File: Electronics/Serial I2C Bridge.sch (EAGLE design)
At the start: 22 parts, among them IC1 ATmega328P, Q1 16MHz

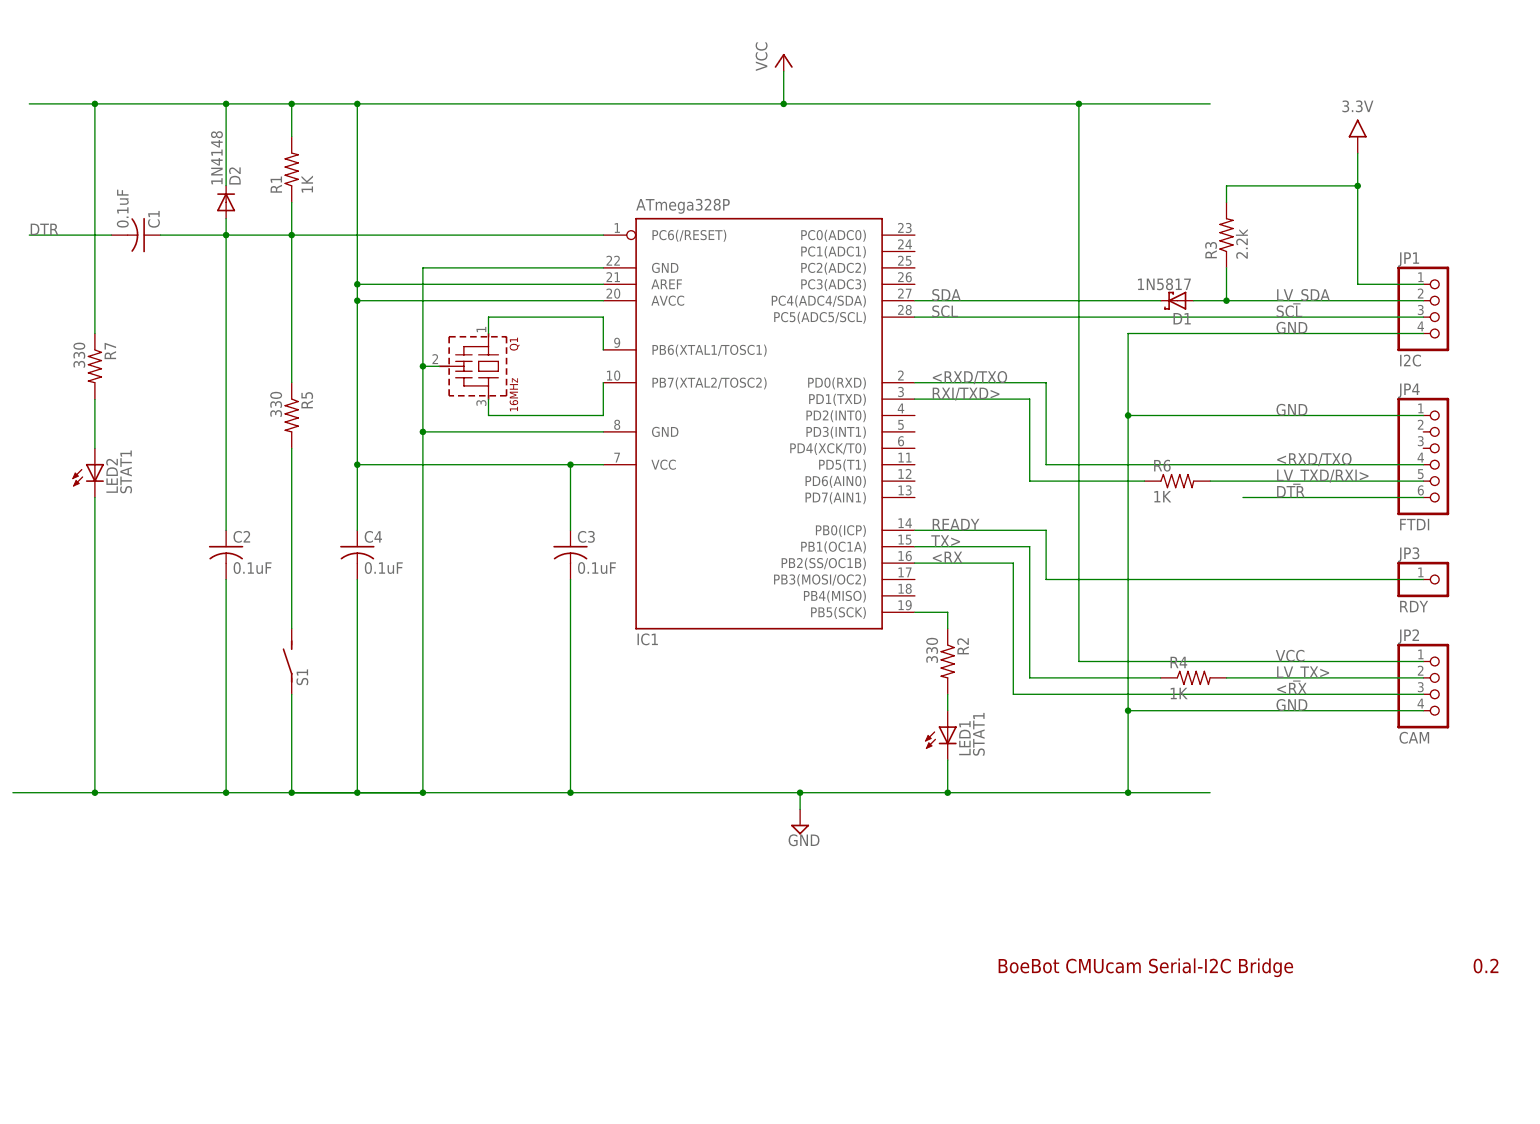
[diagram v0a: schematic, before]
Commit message: Revised level shift circuit
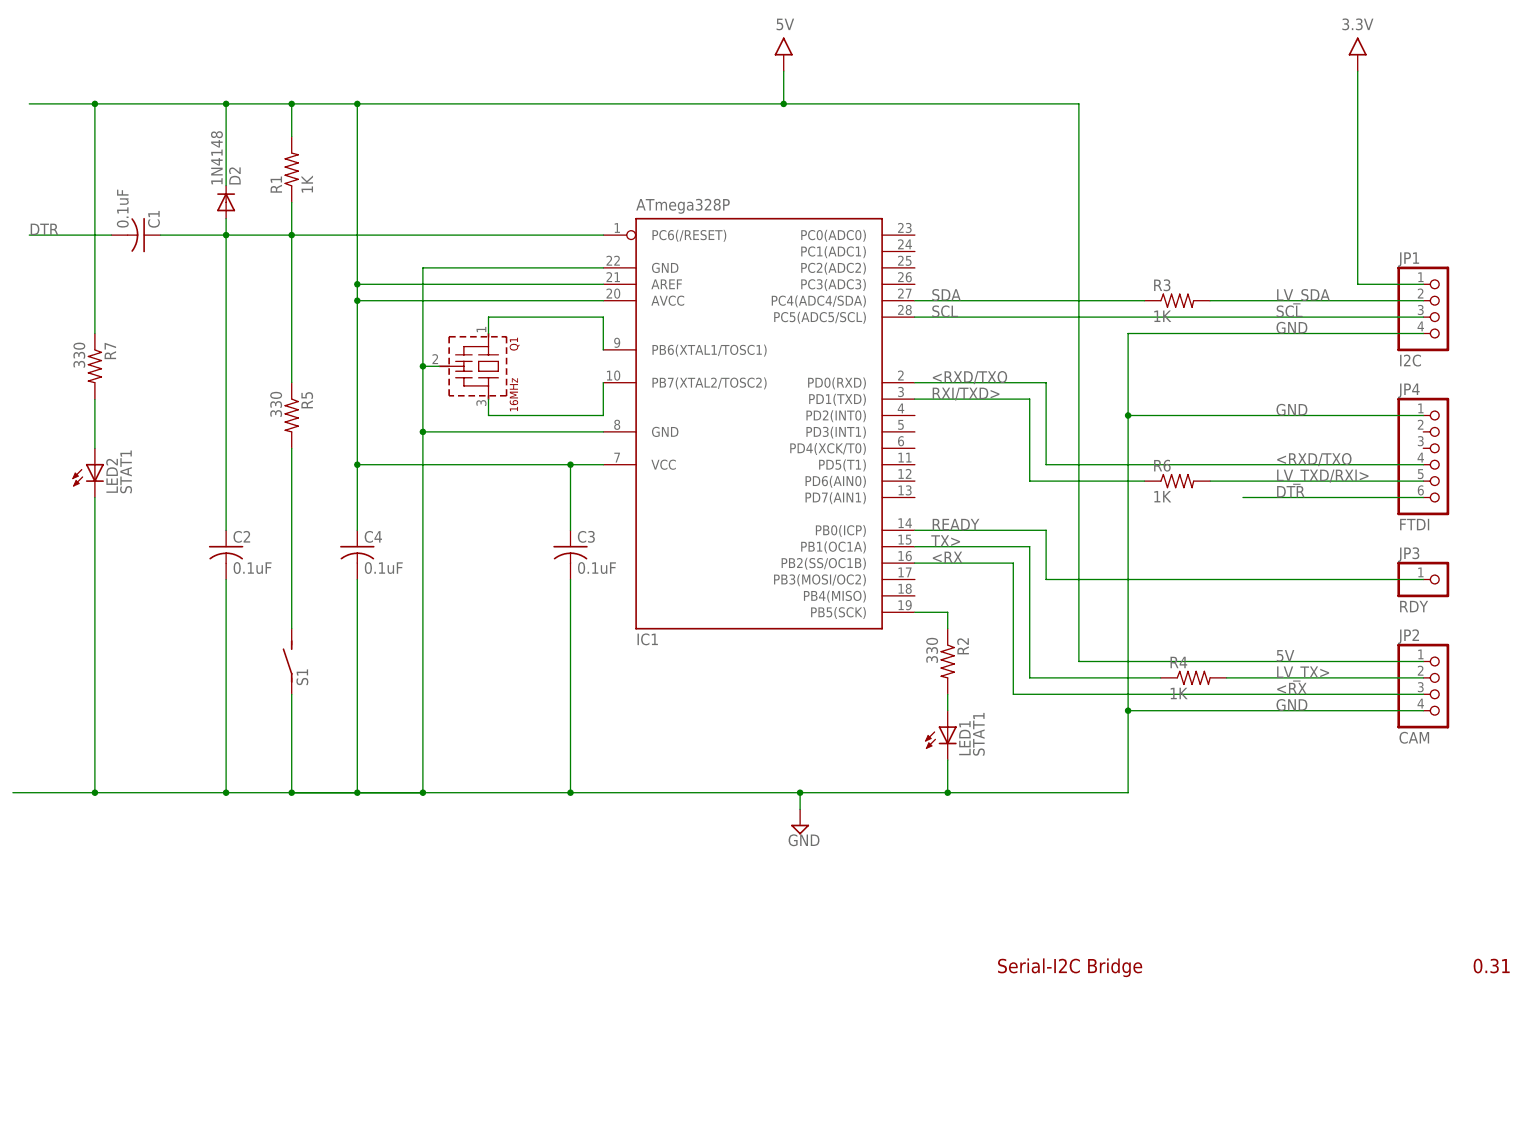
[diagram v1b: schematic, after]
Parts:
- removed D1: 1N5817, diode:1N5817-B
- R3: value 2.2k -> 1K
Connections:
- net VCC renamed 5V
- net 3.3V: no longer R3.2
- net LV_SDA: now also R3.2; no longer D1.A, R3.1
- net SDA: now also R3.1; no longer D1.C
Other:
- note added: "0.31"
- note added: "Serial-I2C Bridge"
- note removed: "0.2"
- note removed: "BoeBot CMUcam Serial-I2C Bridge"
- moved on the sheet: R3

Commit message: Moved RC Mux to subdirectory. Minor changes to various other boards.
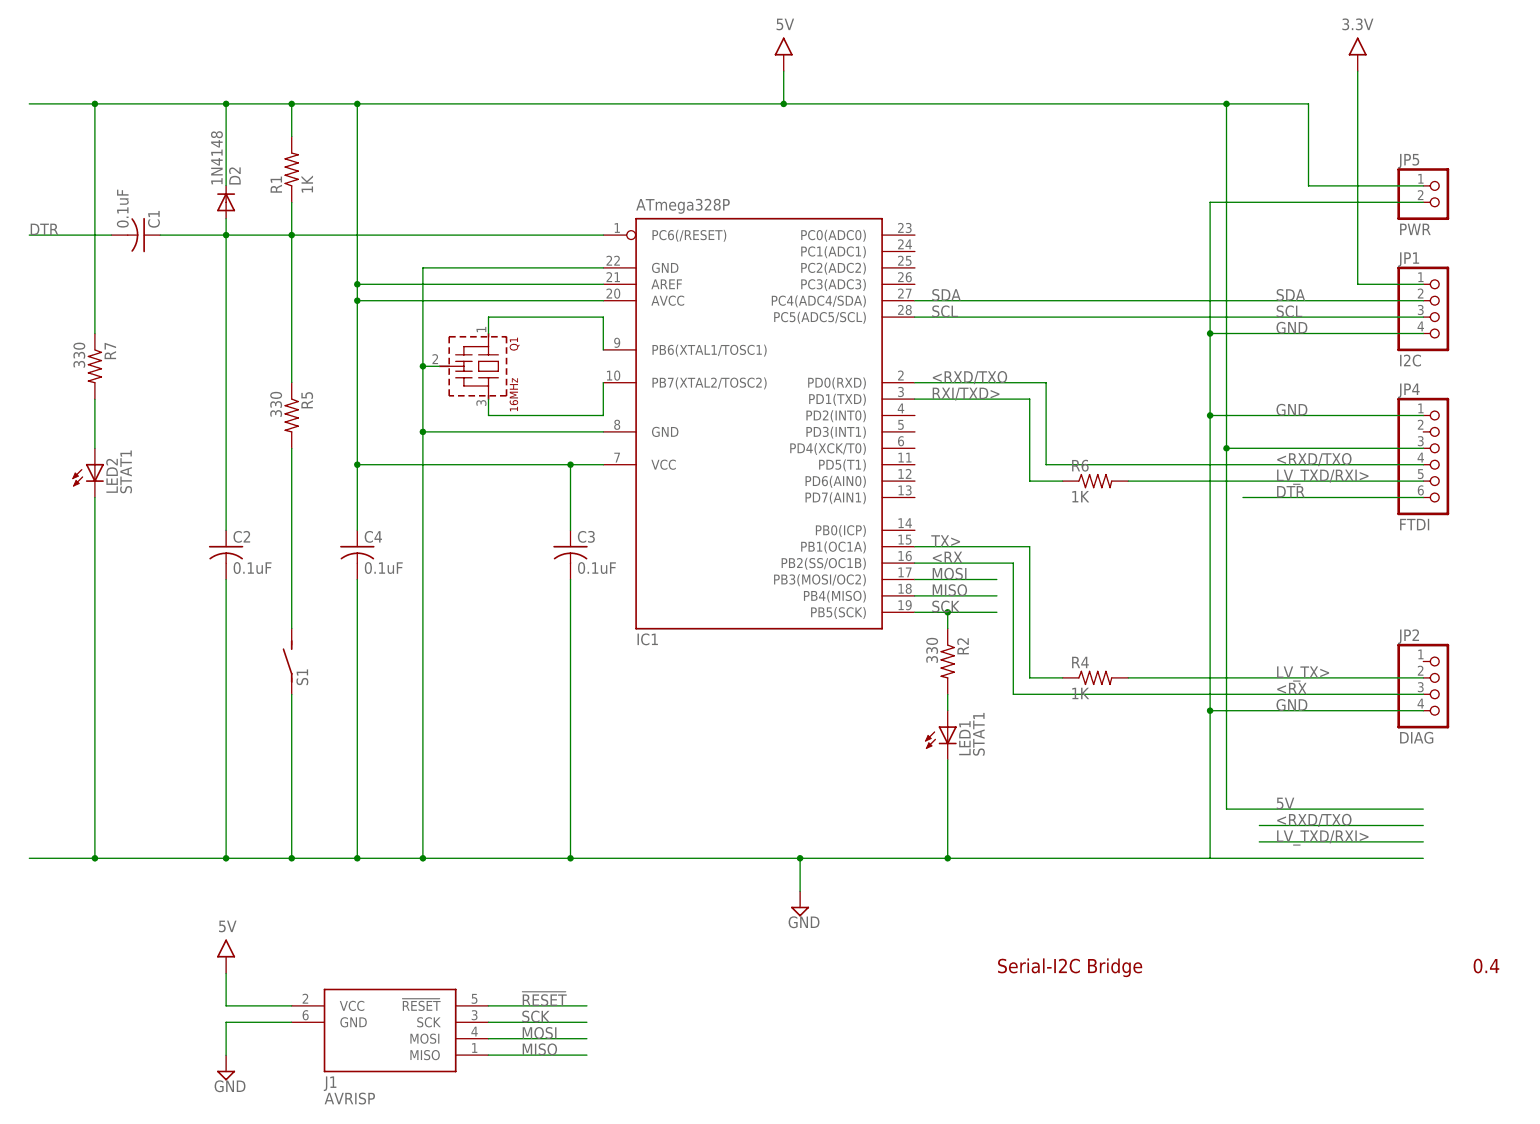
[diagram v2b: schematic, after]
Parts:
- removed JP3: RDY, pinhead-2:PINHD-1X01_2.54-S
- removed R3: 1K, rcl:R-US_0204/5
- added J1: AVRISP, ads4:AVRISP6
- added JP5: PWR, pinhead-2:PINHD-1X02_2.54-S
- JP2: value CAM -> DIAG
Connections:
- removed net LV_SDA: JP1.2, R3.2
- removed net N$5: IC1.PB5(SCK), R2.1
- removed net N$6: C1.1, C2.1, D2.A, IC1.PC6(/RESET), R1.1, R5.1
- removed net READY: IC1.PB0(ICP), JP3.1
- new net !RESET: C1.1, C2.1, D2.A, IC1.PC6(/RESET), J1.!RESET, R1.1, R5.1
- new net MISO: IC1.PB4(MISO), J1.MISO
- new net MOSI: IC1.PB3(MOSI/OC2), J1.MOSI
- new net SCK: IC1.PB5(SCK), J1.SCK, R2.1
- net 5V: now also J1.VCC, JP4.3, JP5.1; no longer JP2.1
- net GND: now also J1.GND, JP5.2
- net SDA: now also JP1.2; no longer R3.1
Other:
- note added: "0.4"
- note removed: "0.31"
- moved on the sheet: R4, R6
